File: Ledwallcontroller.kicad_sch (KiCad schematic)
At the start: 0 parts

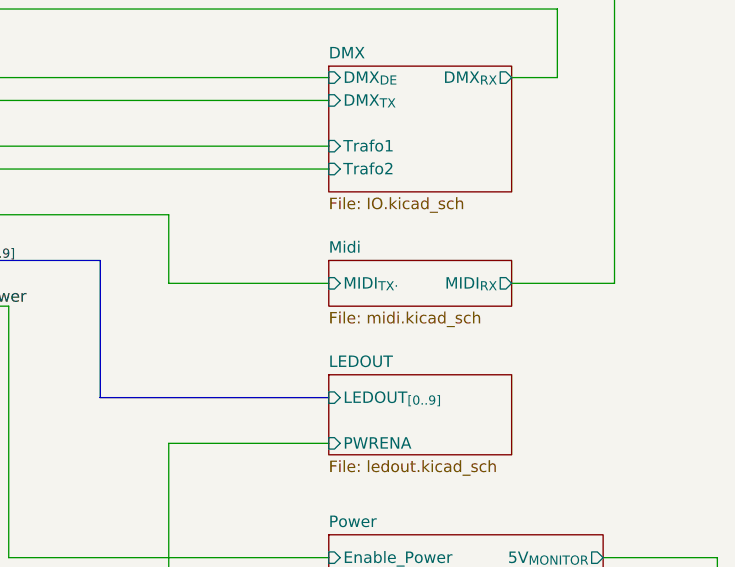
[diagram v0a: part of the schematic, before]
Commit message: Added Testpoints
Schematic and PCB updated
Also probably some other smaller changes that I forgot about
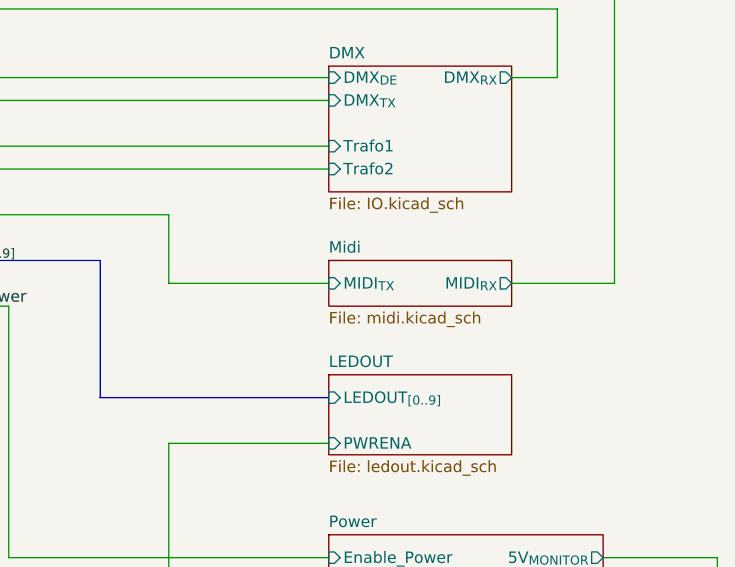
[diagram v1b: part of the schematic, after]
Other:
- sheet Midi ports: added MIDI_{TX}; removed MIDI_{TX·}
